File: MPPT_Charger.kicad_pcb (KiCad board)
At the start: 2 copper layers, 86.8 x 60.8 mm, 118 parts, among them J1 Solar, J2 Battery, J3 USB_B_Mini, J4 INTERFACE PORT, J6 JTAG, J8 Micro_SD_Card_Det_Hirose_DM3AT, J9 IIC RTC, Q1 CSD19505KCS, Q11 CSD19505KCS, Q12 CSD19505KCS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

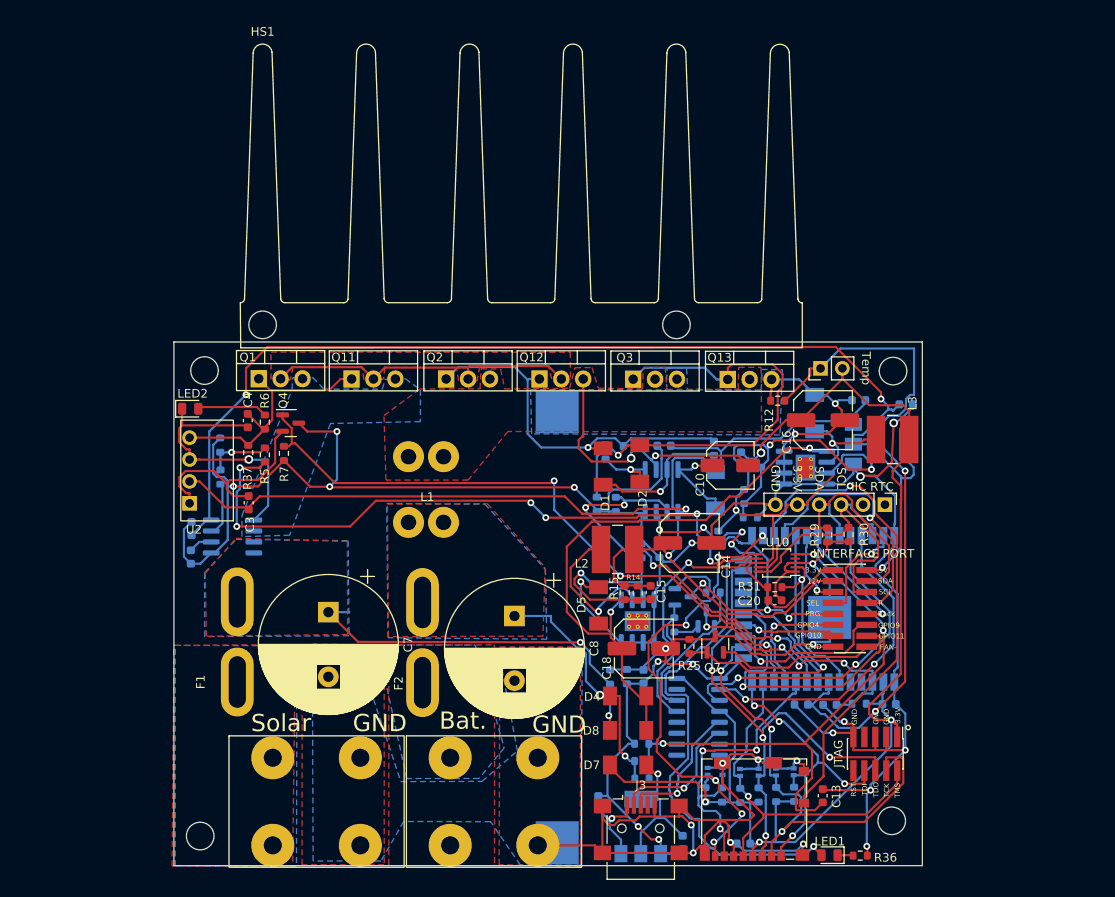
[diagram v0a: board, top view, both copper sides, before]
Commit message: Reworked layout. Changed a few pins. Double power transistors removed. Traces would not be able to support the amperage anyway.
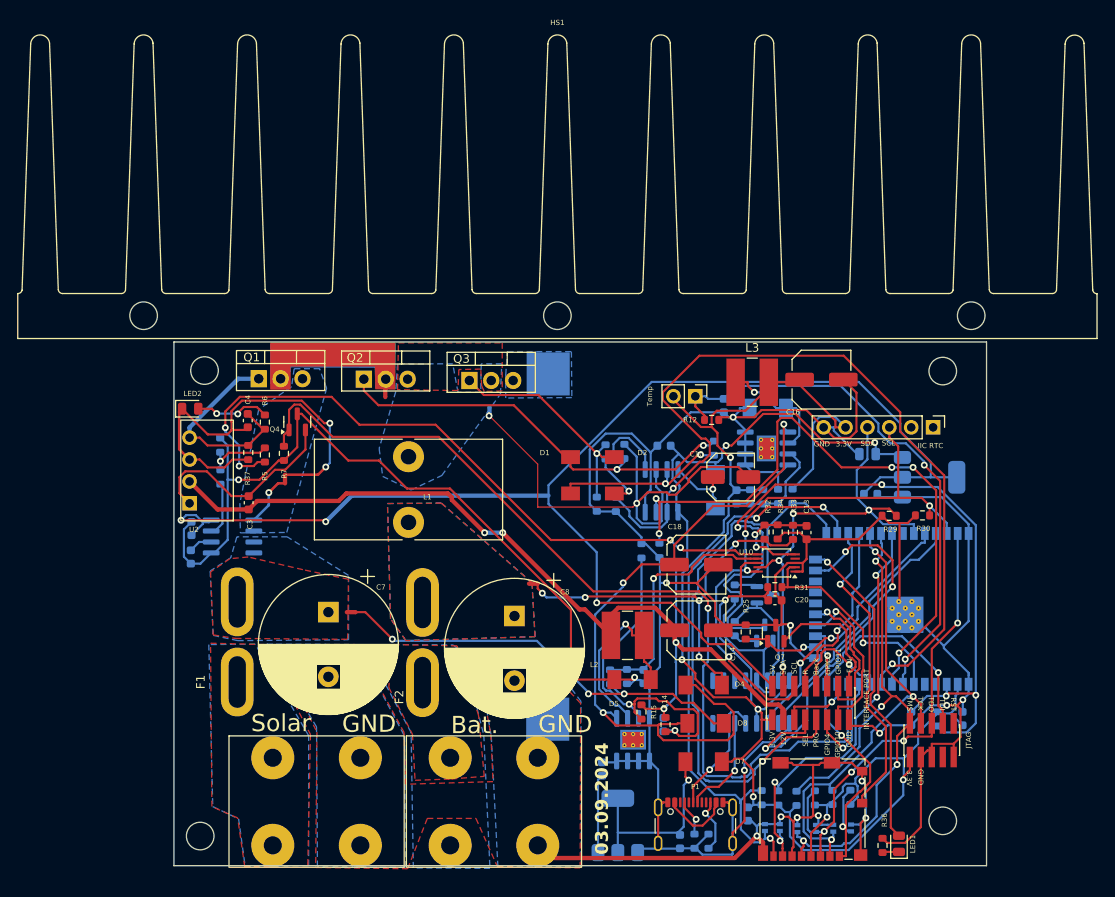
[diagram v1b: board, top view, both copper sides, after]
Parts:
- removed J3: USB_B_Mini, Connector_USB:USB_Mini-B_Lumberg_2486_01_Horizontal
- removed Q11, Q12: CSD19505KCS, Package_TO_SOT_THT:TO-220-3_Vertical
- removed Q13: CSD19505KCS, Library:TO-220-3_Vertical_Insulated
- added NT1: GND to GND2, NetTie:NetTie-2_SMD_Pad0.5mm, F.Cu at (123.7, 133.9)
- added NT2: NetTie_2, NetTie:NetTie-2_SMD_Pad0.5mm, F.Cu at (99.0, 125.5)
- added NT3: NetTie_2, NetTie:NetTie-2_SMD_Pad0.5mm, F.Cu at (91.3, 110.1)
- added NT4: NetTie_2, NetTie:NetTie-2_SMD_Pad0.5mm, B.Cu at (115.1, 102.3)
- added NT5: NetTie_2, NetTie:NetTie-2_SMD_Pad0.5mm, F.Cu at (103.0, 100.1)
- added NT6: NetTie_2, NetTie:NetTie-2_SMD_Pad0.5mm, F.Cu at (120.2, 122.2)
- added P1: USB-C, Connector_USB:USB_C_Receptacle_GCT_USB4105-xx-A_16P_TopMnt_Horizontal, F.Cu at (138.9, 151.3)
- added R41: 5.1K, Resistor_SMD:R_0603_1608Metric, B.Cu at (138.8, 152.1)
- added R42: 5.1K, Resistor_SMD:R_0603_1608Metric, B.Cu at (140.5, 152.1)
- C15: moved to B.Cu
- C5: footprint Capacitor_SMD:C_0603_1608Metric -> Capacitor_SMD:C_0805_2012Metric
- F1, F2: footprint Fuse:Fuse_Blade_ATO_directSolder -> Library:Fuse_Blade_ATO_directSolder
- J8: footprint AA:microSD_HC_Molex_104031-0811 -> Library:microSD_HC_Molex_104031-0811
- Q3: footprint Library:TO-220-3_Vertical_Insulated -> Library:Package_TO_SOT_THTTO-220-3_Vertical_Insulated
- R32, R33, R34: moved to F.Cu
- moved C12 35.8 mm to (142.2, 101.6), turned to -90 degrees
- moved HS1 34.2 mm to (122.9, 91.1)
- moved R32 31.9 mm to (147.0, 116.2), turned to 90 degrees
- moved R33 31.8 mm to (150.3, 116.3), turned to 90 degrees
- moved C13 30.6 mm to (151.8, 116.3), turned to -90 degrees
- moved R34 29.2 mm to (148.5, 116.2), turned to -90 degrees
- moved Q3 19.0 mm to (112.7, 98.7)
- moved L3 17.6 mm to (145.5, 98.9)
- moved R14 15.6 mm to (135.5, 138.6)
- moved C15 15.4 mm to (135.3, 138.6)
- moved R35 14.9 mm to (138.9, 100.5), turned to -90 degrees
- moved JP1 14.4 mm to (121.8, 112.9)
- moved R15 14.0 mm to (132.7, 137.1)
- moved U5 13.8 mm to (131.7, 140.3)
- moved J4 11.9 mm to (152.3, 136.1), turned to 90 degrees
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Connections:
- C10 pad 2: Net-(C10-Pad2) -> Net-(U7-VS)
- C4 pad 2: Net-(C4-Pad2) -> Net-(LED2-K)
- D4 pad 2: Net-(C8-Pad1) -> Net-(D4-A)
- D8 pad 2: Net-(C7-Pad1) -> Net-(D8-A)
- JP1 pad 2: GND -> Net-(JP1-B)
- L1 pad 1: Net-(C10-Pad2) -> Net-(Q2-S)
- LED2 pad 1: Net-(C4-Pad2) -> Net-(LED2-K)
- Q1 pad 3: Net-(C4-Pad2) -> Net-(Q1-S)
- Q2 pad 3: Net-(C10-Pad2) -> Net-(Q2-S)
- Q3 pad 2: Net-(C10-Pad2) -> Net-(Q2-S)
- Q3 pad 3: GND -> Net-(JP1-B)
- R1 pad 1: Net-(C7-Pad1) -> Net-(D8-A)
- R32 pad 1: Net-(C8-Pad1) -> Net-(D4-A)
- R33 pad 1: Net-(C8-Pad1) -> Net-(D4-A)
- R37 pad 1: Net-(C4-Pad2) -> Net-(LED2-K)
- R8 pad 2: Net-(C10-Pad2) -> Net-(U7-VS)
- U1 pad 1: Net-(C4-Pad2) -> Net-(Q1-S)
- U1 pad 2: Net-(C4-Pad2) -> Net-(Q1-S)
- U2 pad 3: Net-(C4-Pad2) -> Net-(LED2-K)
- U7 pad 6: Net-(C10-Pad2) -> Net-(U7-VS)
- U8 pad 10: SD_DAT0 -> KEY_BACK
- U8 pad 13: SD_CLK -> KEY_LEFT
- U8 pad 16: SD_DAT3 -> FAN
- U8 pad 23: SD_CMD -> KEY_SELECT
- U8 pad 29: FAN -> SD_DAT3
- U8 pad 30: KEY_LEFT -> SD_CLK
- U8 pad 31: KEY_BACK -> SD_DAT0
- U8 pad 37: KEY_SELECT -> SD_CMD
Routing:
- net EN: track 31.7 -> 93.9 mm
- net Net-(U7-VS): track 0.00 -> 58.9 mm, vias 0 -> 2
- net A1: track 65.8 -> 12.9 mm, vias 3 -> 2
- net Net-(D8-A): track 0.00 -> 50.3 mm, vias 0 -> 3
- net GND: track 386.3 -> 436.1 mm, vias 22 -> 9
- net DRV_IN: track 48.6 -> 97.9 mm, vias 4 -> 2
- net Net-(LED2-K): track 0.00 -> 49.0 mm, vias 0 -> 2
- net Net-(D4-A): track 0.00 -> 47.1 mm, vias 0 -> 5
- net Net-(C7-Pad1): track 44.9 -> 0.00 mm, vias 2 -> 0
- net PRG: track 33.4 -> 72.0 mm, vias 3 -> 1
- net DRV_SD: track 38.0 -> 74.5 mm, vias 4 -> 5
- net KEY_SELECT: track 12.3 -> 47.0 mm, vias 1 -> 3
- net Net-(C10-Pad2): track 32.4 -> 0.00 mm, vias 2 -> 0
- net BCCU: track 76.7 -> 108.7 mm, vias 3 -> 1
- net Net-(C4-Pad2): track 31.3 -> 0.00 mm, vias 1 -> 0
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- added copper zone on B.Cu, net Net-(JP1-B)
- added copper zone on B.Cu, net Net-(Q1-S)
- added copper zone on B.Cu, net Net-(Q2-S)
- added copper zone on F.Cu, net Net-(Q2-S)
- removed copper zone on B.Cu, net GND
- removed copper zone on F.Cu, net Net-(C10-Pad2)
- removed copper zone on B.Cu, net Net-(C4-Pad2)
- removed copper zone on F.Cu, net Net-(Q1-D)
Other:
- board size 86.8 x 60.8 mm -> 94.3 x 60.8 mm
- board text added: "03.09.2024"

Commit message: Some manual corrections, and some too small footprints updated.
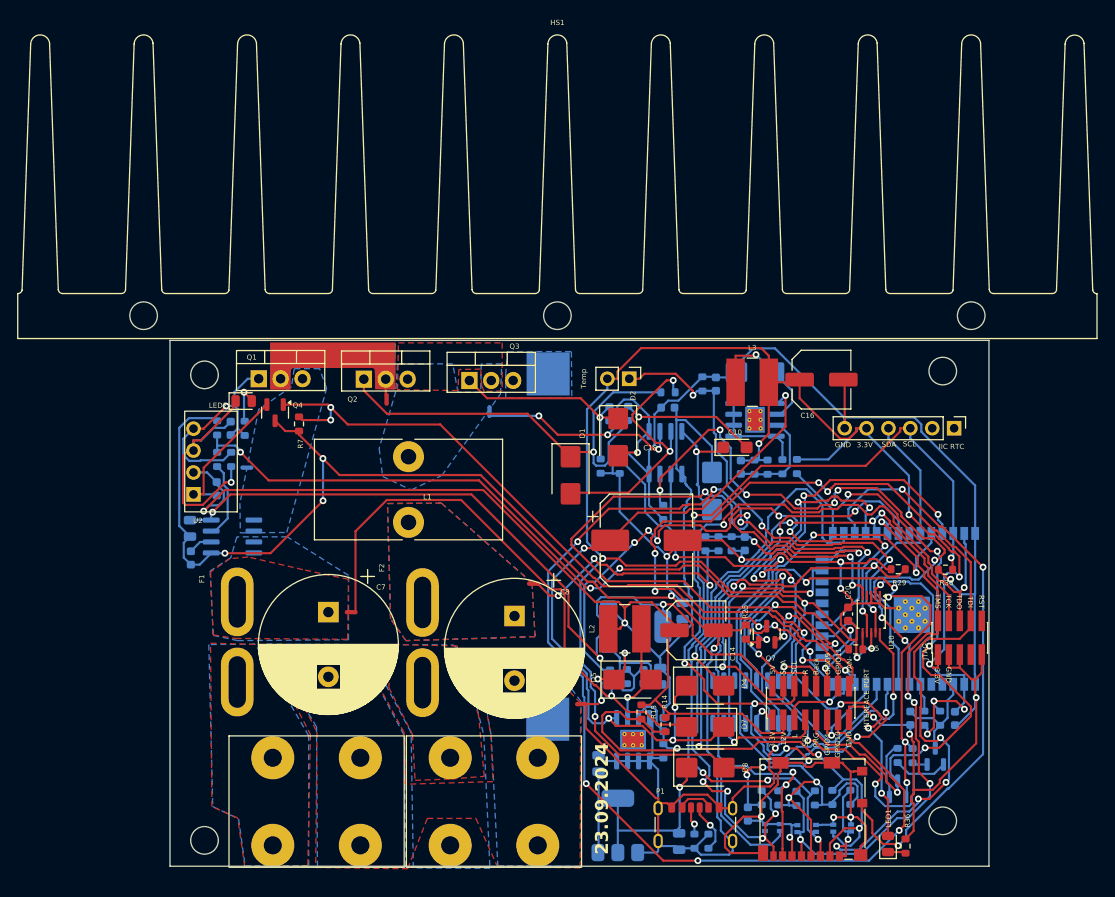
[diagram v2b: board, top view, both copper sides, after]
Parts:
- C10: footprint Capacitor_SMD:C_Elec_5x5.4 -> Capacitor_Tantalum_SMD:CP_EIA-3216-10_Kemet-I
- C13, C3, C4, NT3, R12, R31, R32, R33, R34, R37, R6: moved to B.Cu
- C18: footprint Capacitor_SMD:C_Elec_6.3x5.8 -> Capacitor_SMD:CP_Elec_10x10.5
- C21, C22, C6, C9: footprint Capacitor_SMD:C_0603_1608Metric -> Capacitor_SMD:C_0805_2012Metric
- D1, D2, D3, D4, D5, D6, D7, D8: footprint AA:DO-214AA -> Diode_SMD:D_SMB
- P1: footprint Connector_USB:USB_C_Receptacle_GCT_USB4105-xx-A_16P_TopMnt_Horizontal -> Connector_USB:USB_C_Receptacle_GCT_USB4125-xx-x_6P_TopMnt_Horizontal
- moved R5 72.2 mm to (157.5, 129.8), turned to 180 degrees
- moved U3 38.2 mm to (132.0, 127.2)
- moved C5 35.2 mm to (134.9, 133.0), turned to -90 degrees
- moved Q6 27.3 mm to (162.4, 146.0), turned to 90 degrees
- moved R23 26.8 mm to (162.4, 142.2)
- moved C6 25.7 mm to (137.5, 125.4), turned to 90 degrees
- moved R22 25.3 mm to (164.1, 142.2)
- moved Q5 24.4 mm to (166.8, 142.3)
- moved R16 23.4 mm to (135.2, 141.6), turned to -90 degrees
- moved R31 23.1 mm to (165.5, 137.8), turned to 90 degrees
- moved U10 12.5 mm to (159.3, 125.8), turned to -90 degrees
- moved J6 12.3 mm to (169.6, 128.5)
- moved R33 10.2 mm to (140.1, 117.6)
- moved C20 8.64 mm to (156.7, 125.7), turned to -90 degrees
- moved R9 8.38 mm to (135.8, 100.0), turned to 180 degrees
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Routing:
- net GPIO10: track 19.4 -> 141.7 mm, vias 1 -> 7
- net +3.3V: track 207.3 -> 293.4 mm, vias 7 -> 19
- net SD_DAT2: track 54.5 -> 138.3 mm, vias 3 -> 12
- net EN: track 93.9 -> 12.5 mm, vias 4 -> 0
- net Net-(R3-Pad2): track 7.87 -> 87.6 mm, vias 1 -> 3
- net Net-(LED1-A): track 37.0 -> 116.1 mm, vias 1 -> 7
- net A2: track 80.3 -> 1.94 mm, vias 4 -> 0
- net GND: track 436.1 -> 511.1 mm, vias 9 -> 18
- net +5V: track 157.9 -> 98.2 mm
- net SCL: track 67.8 -> 118.6 mm, vias 4 -> 5
- net SD_CMD: track 53.9 -> 102.4 mm, vias 4 -> 5
- net A3: track 28.7 -> 76.4 mm, vias 1 -> 7
- net SD_DAT3: track 54.5 -> 99.7 mm, vias 3 -> 6
- net Net-(Q6-E): track 17.7 -> 61.5 mm, vias 0 -> 5
- net SD_DAT0: track 48.9 -> 84.8 mm
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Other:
- board size 94.3 x 60.8 mm -> 95 x 61 mm
- board text added: "23.09.2024"
- board text removed: "03.09.2024"

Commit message: A lot of updates. Used net classes. Changed some footprints and 3D models. Corrected pinouts of connectors. Changed pins for keyboard to use same pins as JTAG connector, seemed like a useful double use that should not collide, and I am running out of GPIOs soon.
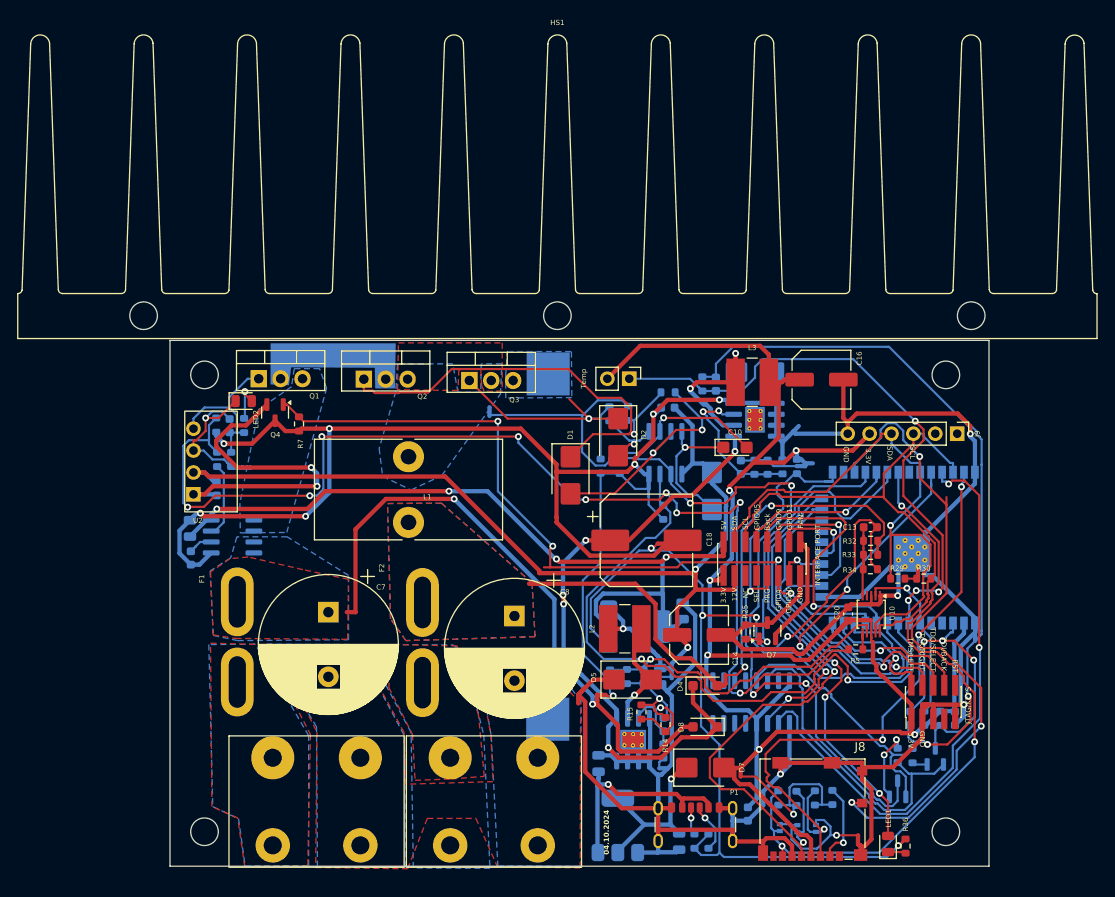
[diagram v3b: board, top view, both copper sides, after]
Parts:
- removed D13, D14, D9: LESD8D3.3CAT5G, AA:SOD882D.kicad_mod
- removed R26, R40: 10k, Resistor_SMD:R_0603_1608Metric
- added NT10: NetTie_2, NetTie:NetTie-2_SMD_Pad0.5mm, F.Cu at (142.4, 133.3)
- added NT11: NetTie_2, NetTie:NetTie-2_SMD_Pad0.5mm, B.Cu at (135.3, 143.6)
- added NT12: NetTie_2, NetTie:NetTie-2_SMD_Pad0.5mm, B.Cu at (136.2, 132.7)
- added NT13: NetTie_2, NetTie:NetTie-2_SMD_Pad0.5mm, B.Cu at (151.2, 108.6)
- added NT14: NetTie_2, NetTie:NetTie-2_SMD_Pad0.5mm, F.Cu at (164.8, 120.8)
- added NT15: NetTie_2, NetTie:NetTie-2_SMD_Pad0.5mm, B.Cu at (171.4, 128.4)
- added NT16: NetTie_2, NetTie:NetTie-2_SMD_Pad0.5mm, F.Cu at (157.8, 151.9)
- added NT17: NetTie_2, NetTie:NetTie-2_SMD_Pad0.5mm, B.Cu at (133.5, 110.7)
- added NT7: ~, NetTie:NetTie-2_SMD_Pad0.5mm, F.Cu at (135.1, 117.6)
- added NT8: ~, NetTie:NetTie-2_SMD_Pad0.5mm, F.Cu at (144.2, 144.1)
- added NT9: NetTie_2, NetTie:NetTie-2_SMD_Pad0.5mm, F.Cu at (128.0, 135.1)
- C13, R32, R33, R34: moved to F.Cu
- D4, D8: footprint Diode_SMD:D_SMB -> Diode_SMD:D_SOD-123F
- J6: value JTAG -> JTAG/KEYS
- NT5: moved to B.Cu
- moved R33 19.2 mm to (159.3, 118.9), turned to 180 degrees
- moved J4 17.7 mm to (146.7, 119.3)
- moved R32 17.6 mm to (159.3, 117.2), turned to 180 degrees
- moved R34 16.4 mm to (159.2, 120.5), turned to 0 degrees
- moved C13 14.7 mm to (159.2, 115.7), turned to 0 degrees
- moved J6 8.08 mm to (166.5, 136.0)
- moved U8 7.10 mm to (163.1, 118.0)
- moved NT5 4.32 mm to (103.0, 96.5), turned to -90 degrees
- moved R30 2.72 mm to (165.4, 121.6)
- moved REF2 1.32 mm to (168.0, 151.0)
- moved R29 1.09 mm to (162.4, 121.6), turned to 180 degrees
- moved REF1 1.00 mm to (82.0, 151.0)
- moved J9 0.73 mm to (169.3, 104.8)
- moved NT1 0.70 mm to (125.3, 135.6), turned to 90 degrees
- moved C14 0.61 mm to (139.4, 128.2)
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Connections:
- net Net-(U8-IO35) renamed Utemp
- net SD_DAT0 renamed SD_MISO
- C1 pad 2: GND -> Net-(C1-Pad2)
- C12 pad 2: GND -> GND_U8
- C13 pad 2: GND -> GND_LP
- C15 pad 1: +12V -> Net-(C15-Pad1)
- C17 pad 1: +3.3V -> Net-(C17-Pad1)
- C19 pad 1: GND -> GND_U8
- C24 pad 2: GND2 -> GND
- D10 pad 1: GND2 -> Net-(D10-A1)
- D11 pad 1: GND2 -> Net-(D10-A1)
- D12 pad 1: GND2 -> Net-(D10-A1)
- D12 pad 2: SD_CMD -> SD_MOSI
- J4 pad 10: KEY_BACK -> GPIO25
- J4 pad 5: KEY_LEFT -> unconnected-(J4-Pin_5-Pad5)
- J4 pad 7: KEY_SELECT -> unconnected-(J4-Pin_7-Pad7)
- J4 pad 8: KEY_RIGHT -> GPIO5
- J6 pad 2: SD_CLK -> KEY_LEFT
- J6 pad 4: SD_DAT3 -> KEY_RIGHT
- J6 pad 6: SD_CMD -> KEY_SELECT
- J6 pad 8: SD_DAT2 -> KEY_BACK
- J8 pad 1: SD_DAT2 -> unconnected-(J8-DAT2-Pad1)
- J8 pad 10: GND2 -> GND
- J8 pad 11: GND2 -> GND
- J8 pad 2: SD_DAT3 -> Net-(J8-DAT3/CD)
- J8 pad 3: SD_CMD -> SD_MOSI
- J8 pad 6: GND2 -> GND
- J8 pad 8: SD_DAT1 -> unconnected-(J8-DAT1-Pad8)
- NT1 pad 1: GND -> GND2
- NT1 pad 2: GND2 -> GND
- P1 pad A9: Net-(P1-VBUS-PadA4) -> VBUS
- P1 pad B9: Net-(P1-VBUS-PadA4) -> VBUS
- R1 pad 1: Net-(D8-A) -> Net-(NT9-Pad2)
- R11 pad 2: GND -> Net-(C1-Pad2)
- R12 pad 2: GND -> GND_U8
- R13 pad 2: GND -> Net-(C1-Pad2)
- R14 pad 1: +12V -> Net-(C15-Pad1)
- R15 pad 1: +12V -> Net-(C15-Pad1)
- R16 pad 2: GND -> Net-(NT11-Pad2)
- R17 pad 1: +3.3V -> Net-(C17-Pad1)
- R18 pad 1: +3.3V -> Net-(C17-Pad1)
- R2 pad 2: GND -> Net-(C1-Pad2)
- R20 pad 2: GND -> Net-(C1-Pad2)
- R27 pad 1: +3.3V -> +3.3V_LP
- R28 pad 1: +3.3V -> +3.3V_LP
- R29 pad 1: GND -> GND_J4
- R30 pad 1: GND -> GND_J4
- R32 pad 1: Net-(D4-A) -> Net-(NT10-Pad2)
- R33 pad 1: Net-(D4-A) -> Net-(NT10-Pad2)
- R34 pad 2: GND -> GND_LP
- R36 pad 1: GND -> GND_LP
- R38 pad 1: +3.3V -> +3.3V_LP
- R38 pad 2: SD_CMD -> SD_MOSI
- R39 pad 1: +3.3V -> +3.3V_LP
- R39 pad 2: SD_DAT3 -> Net-(J8-DAT3/CD)
- R41 pad 2: GND -> GND_LP
- R42 pad 2: GND -> GND_LP
- U3 pad 1: GND -> GND_LP
- U8 pad 10: KEY_BACK -> GPIO25
- U8 pad 14: SD_DAT2 -> KEY_BACK
- U8 pad 16: FAN -> KEY_RIGHT
- U8 pad 28: KEY_RIGHT -> FAN
- U8 pad 29: SD_DAT3 -> GPIO5
- U8 pad 37: SD_CMD -> SD_MOSI
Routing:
- net SD_DAT2: track 138.3 -> 0.00 mm, vias 12 -> 0
- net GPIO10: track 141.7 -> 6.38 mm, vias 7 -> 1
- net GND_LP: track 0.00 -> 124.7 mm, vias 0 -> 5
- net SD_CMD: track 102.4 -> 0.00 mm, vias 5 -> 0
- net SD_DAT3: track 99.7 -> 0.00 mm, vias 6 -> 0
- net +3.3V: track 293.4 -> 207.5 mm, vias 19 -> 6
- net GND_U8: track 0.00 -> 84.1 mm, vias 0 -> 2
- net SD_DAT1: track 74.3 -> 0.00 mm, vias 4 -> 0
- net SD_MOSI: track 0.00 -> 71.9 mm, vias 0 -> 4
- net Net-(LED1-A): track 116.1 -> 49.4 mm, vias 7 -> 3
- net SCL: track 118.6 -> 60.3 mm, vias 5 -> 0
- net GND2: track 55.8 -> 0.00 mm, vias 4 -> 0
- net GND: track 511.1 -> 461.9 mm, vias 18 -> 11
- net Net-(R3-Pad2): track 87.6 -> 131.7 mm, vias 3 -> 9
- net Net-(NT10-Pad2): track 0.00 -> 43.0 mm, vias 0 -> 2
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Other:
- board text added: "04.10.2024"
- board text removed: "23.09.2024"
